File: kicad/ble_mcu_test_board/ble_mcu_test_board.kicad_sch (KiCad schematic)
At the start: 22 parts, among them J1 I2C, J2 SWD, U1 STM32WB10CCUx, U2 DLF162500LT-5028A1, Y1 32MHz

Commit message: prototype mobo progress
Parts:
- removed J1: I2C, symbol Connector:Conn_01x04_Pin
- removed J2: SWD, symbol Connector:Conn_01x04_Pin
- added AE1: Antenna, symbol Device:Antenna
- added C16: 0.3p, symbol Device:C
- added C17: 0.8p, symbol Device:C
- added C18, C19: 22u, symbol Device:C
- added J2: SWD, symbol Connector:Conn_01x04_Socket
- added J3: USB_C_Receptacle_PowerOnly_6P, symbol Connector:USB_C_Receptacle_PowerOnly_6P
- added J4: I2C_MUX_OUT, symbol Connector_Generic:Conn_02x16_Counter_Clockwise
- added L1: 2.7n, symbol Device:L
- added R3: 4k7, symbol Device:R
- added SW1: SW_SPDT, symbol Switch:SW_SPDT
- added U3: AMS1117-3.3, Package_TO_SOT_SMD:SOT-223-3_TabPin2, symbol Regulator_Linear:AMS1117-3.3
- added U4: TCA9548APWR, PW24_TEX, symbol 2024-09-17_00-23-00:TCA9548APWR
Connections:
- net +3.3V: now also C18.1, J4.12 (Pin_12), J4.16 (Pin_16), J4.17 (Pin_17), J4.21 (Pin_21), J4.25 (Pin_25), J4.29 (Pin_29), J4.4 (Pin_4), J4.8 (Pin_8), R3.1, U3.2 (VO), U4.24 (VCC)
- net GND: now also U2.2 (GND), U2.4 (GND), C16.2, C17.2, C18.2, C19.2, J2.4 (Pin_4), J3.A12 (GND), J3.B12 (GND), J4.1 (Pin_1), J4.13 (Pin_13), J4.20 (Pin_20), J4.24 (Pin_24), J4.28 (Pin_28), J4.32 (Pin_32), J4.5 (Pin_5), J4.9 (Pin_9), U3.1 (GND), U4.1 (A0), U4.12 (GND), U4.2 (A1), U4.21 (A2)
- net RF_OUT: now also C17.1, L1.1
- net at C10.1, C11.1, C4.1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: now also U1.1 (VBAT)
- net +3.3VA: now reaches C12.1, C13.1, U1.8 (VDDA)
- net at U2.1 (IN): now also C16.1, L1.2
- net at U2.3 (OUT): now also AE1.1 (A)
- net at R2.2, U1.6 (PB9): now also U4.23 (SDA)
- net at U1.39 (PA13): now also J2.2 (Pin_2)
- net BOOT0: now reaches U1.4 (PH3)
- net BOOT0: now also SW1.2 (B)
- net at U1.41 (PA14): now also J2.3 (Pin_3)
- net at R1.2, U1.5 (PB8): now also U4.22 (SCL)
- new net: R3.2, U4.3 (*RESET)
- new net: J4.10 (Pin_10), U4.16 (SC5)
- new net: J4.11 (Pin_11), U4.15 (SD5)
- new net: J4.14 (Pin_14), U4.14 (SC4)
- new net: J4.15 (Pin_15), U4.13 (SD4)
- new net: J4.18 (Pin_18), U4.11 (SC3)
- new net: J4.19 (Pin_19), U4.10 (SD3)
- new net: J4.2 (Pin_2), U4.20 (SC7)
- new net: J4.22 (Pin_22), U4.9 (SC2)
- new net: J4.23 (Pin_23), U4.8 (SD2)
- new net: J4.26 (Pin_26), U4.7 (SC1)
- new net: J4.27 (Pin_27), U4.6 (SD1)
- new net: J4.3 (Pin_3), U4.19 (SD7)
- new net: J4.30 (Pin_30), U4.5 (SC0)
- new net: J4.6 (Pin_6), U4.18 (SC6)
- new net: J4.7 (Pin_7), U4.17 (SD6)
- new net +3V3: J2.1 (Pin_1)
- new net VBUS: C19.1, J3.A9 (VBUS), J3.B9 (VBUS), U3.3 (VI)
- no-connect marks 0 -> 1
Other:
- note added: "2.4-2.5GHz LPF"
- note added: "Impedance matching network for QFN48 package STM32WB according to AN5165"
- note added: "POWER DECOUPLING"
- note added: "RF"
- note added: "nVDD x 100 nF + 1 x 4.7 μF"
- note removed: "Decoupling: nVDD x 100 nF + 1 x 4.7 μF"
- company: (none) -> FL24C6 / Posture Best
- title: (none) -> Bluetooth MCU Prototype
- moved on the sheet: C1, C10, C11, C12, C13, C14, C15, C2, C3, C4, C5, C6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

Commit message: finished schematic
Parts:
- added R4: 10k, symbol Device:R
- added SW2: SW_Push, symbol Switch:SW_Push
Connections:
- net +3V3 is gone; now on net +3.3V: J2.1 (Pin_1)
- net +3.3V: now also C10.1, C11.1, C14.1, C15.1, C4.1, C5.1, C6.1, C7.1, C8.1, C9.1, SW1.3 (C), U1.1 (VBAT), U1.20 (VDD), U1.23 (VDDRF), U1.31 (VDD), U1.33 (VDD), U1.34 (VDD), U1.35 (VDD), U1.40 (VDD), U1.48 (VDD)
- net BOOT0: now also R4.1; no longer SW1.2 (B)
- net GND: now also SW1.1 (A), SW2.2
- net at J4.31 (Pin_31): now also U4.4 (SD0)
- net at U1.15 (PA6): now also SW2.1
- new net: R4.2, SW1.2 (B)
- no-connect marks 1 -> 27
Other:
- note added: "BOOT MODE"
- note added: "Button for possible user control. Pulled up internally per STM32CubeIDE config."
- note added: "C1 and C2 must be connected to ground by separate vias."
- note added: "GND = Run code in flash 3.3V = Listen for peripherals"
- note added: "I2C"
- note added: "USB POWER"
- note removed: "C1 and C2 must be connected to ground by a separate via."
- moved on the sheet: C1, C10, C11, C12, C13, C14, C15, C2, C3, C4, C5, C6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

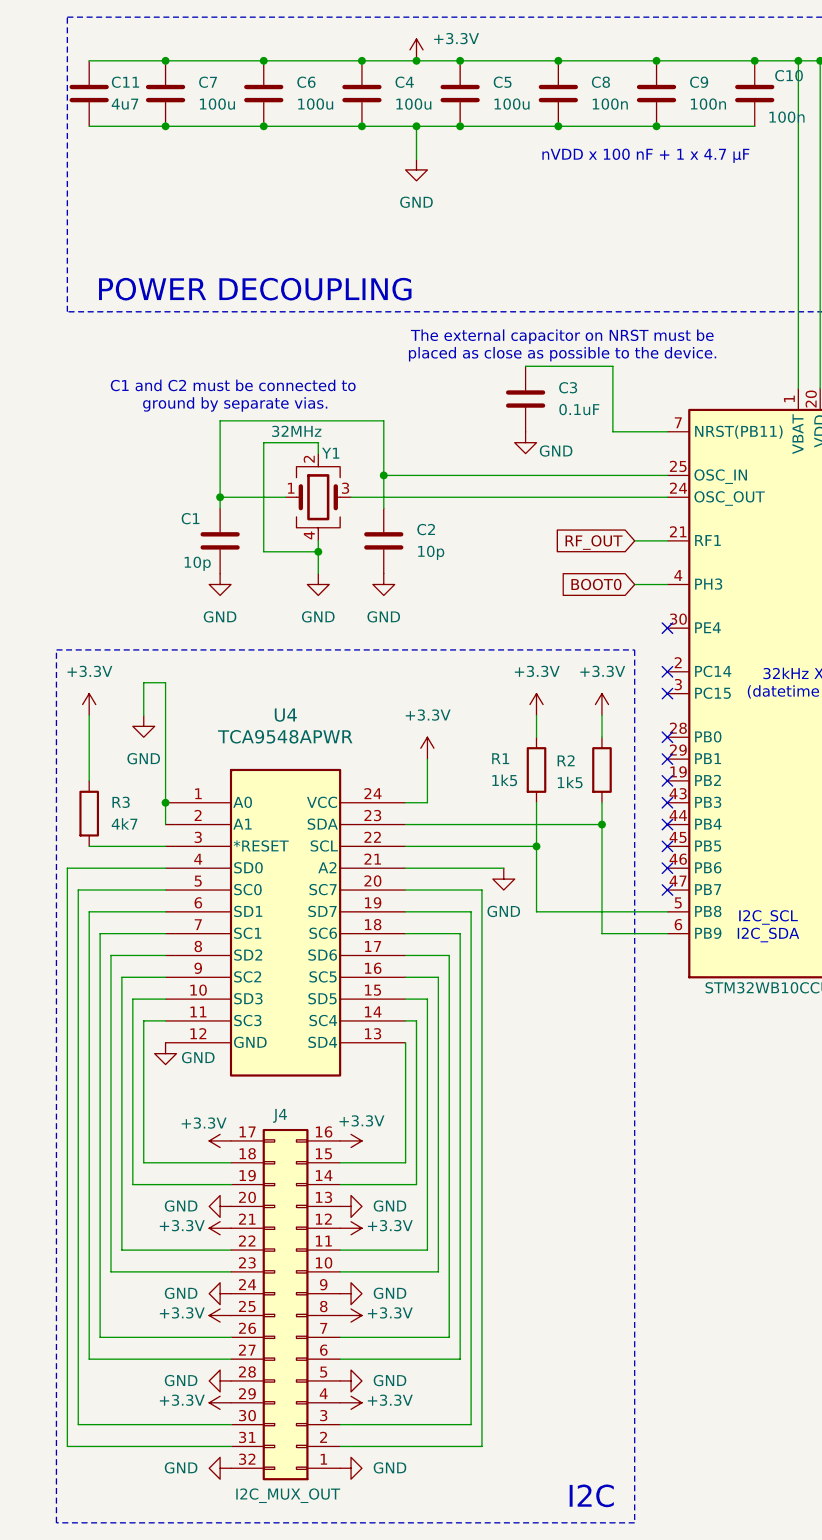
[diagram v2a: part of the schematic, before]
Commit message: reordered i2c multiplexer output, started pcb layout
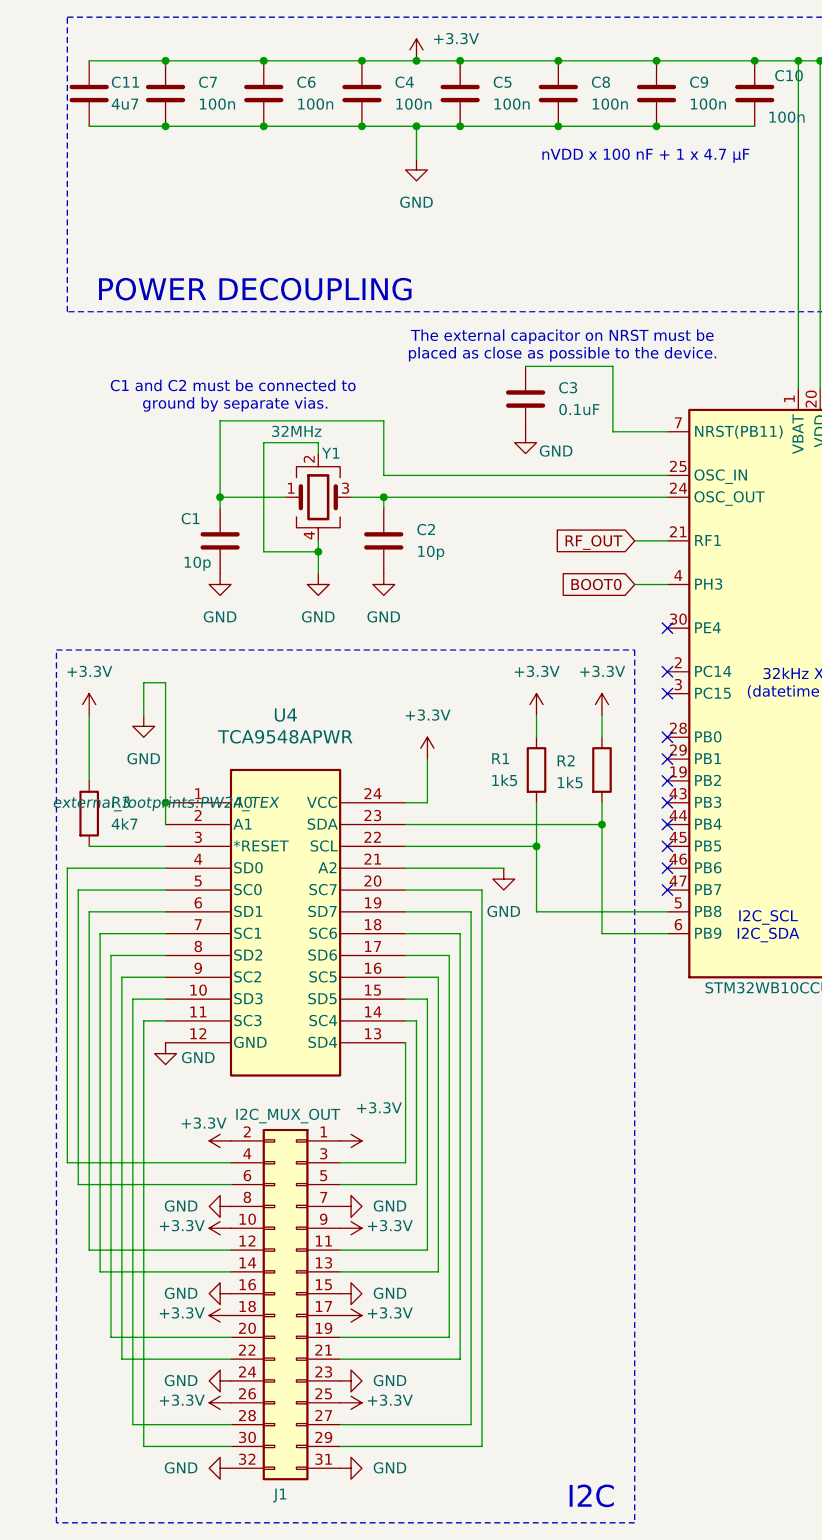
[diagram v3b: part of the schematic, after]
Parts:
- removed J4: I2C_MUX_OUT, symbol Connector_Generic:Conn_02x16_Counter_Clockwise
- added J1: I2C_MUX_OUT, Connector_PinSocket_2.54mm:PinSocket_2x16_P2.54mm_Horizontal, symbol Connector_Generic:Conn_02x16_Odd_Even
- C1, C10, C12, C13, C14, C15, C16, C17, C2, C3, C8, C9: footprint (none) -> Capacitor_SMD:C_0402_1005Metric
- C11: footprint (none) -> Capacitor_SMD:C_0603_1608Metric
- C18, C19: footprint (none) -> Capacitor_SMD:C_0805_2012Metric
- C4, C5, C6, C7: value 100u -> 100n; footprint (none) -> Capacitor_SMD:C_0402_1005Metric
- J2: footprint (none) -> Connector_PinSocket_2.54mm:PinSocket_1x04_P2.54mm_Horizontal
- R4: footprint (none) -> Resistor_SMD:R_0402_1005Metric_Pad0.72x0.64mm_HandSolder
- SW1: footprint (none) -> Button_Switch_SMD:SW_SPDT_PCM12
- SW2: footprint (none) -> Button_Switch_SMD:SW_Push_1P1T-SH_NO_CK_KMR2xxG
- U2: footprint DLF-4_1P6X0P8 -> external_footprints:DLF-4_1P6X0P8
- U4: footprint PW24_TEX -> external_footprints:PW24_TEX
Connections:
- net +3.3V: now also J1.1 (Pin_1), J1.10 (Pin_10), J1.17 (Pin_17), J1.18 (Pin_18), J1.2 (Pin_2), J1.25 (Pin_25), J1.26 (Pin_26), J1.9 (Pin_9)
- net GND: now also J1.15 (Pin_15), J1.16 (Pin_16), J1.23 (Pin_23), J1.24 (Pin_24), J1.31 (Pin_31), J1.32 (Pin_32), J1.7 (Pin_7), J1.8 (Pin_8)
- net at U4.16 (SC5): now also J1.13 (Pin_13)
- net at U4.15 (SD5): now also J1.11 (Pin_11)
- net at U4.14 (SC4): now also J1.5 (Pin_5)
- net at U4.13 (SD4): now also J1.3 (Pin_3)
- net at U4.11 (SC3): now also J1.30 (Pin_30)
- net at U4.10 (SD3): now also J1.28 (Pin_28)
- net at U4.20 (SC7): now also J1.29 (Pin_29)
- net at U4.9 (SC2): now also J1.22 (Pin_22)
- net at U4.8 (SD2): now also J1.20 (Pin_20)
- net at U4.7 (SC1): now also J1.14 (Pin_14)
- net at U4.6 (SD1): now also J1.12 (Pin_12)
- net at U4.19 (SD7): now also J1.27 (Pin_27)
- net at U4.5 (SC0): now also J1.6 (Pin_6)
- net at U4.4 (SD0): now also J1.4 (Pin_4)
- net at U4.18 (SC6): now also J1.21 (Pin_21)
- net at U4.17 (SD6): now also J1.19 (Pin_19)
- net at C1.1, U1.25 (OSC_IN), Y1.1: no longer C2.1
- net at U1.24 (OSC_OUT), Y1.3: now also C2.1

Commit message: prototype schematic + pcb finalized and ordered
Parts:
- added R5, R6: 5k1, Resistor_SMD:R_0603_1608Metric, symbol Device:R
- AE1: footprint (none) -> pcb_antenna:meander_antenna_stm32wb10cc
- J3: footprint (none) -> Connector_USB:USB_C_Receptacle_HRO_TYPE-C-31-M-17
- L1: footprint (none) -> Inductor_SMD:L_0402_1005Metric
- R1, R2: value 1k5 -> 4k7; footprint (none) -> Resistor_SMD:R_0603_1608Metric
- R3: footprint (none) -> Resistor_SMD:R_0402_1005Metric
- R4: footprint Resistor_SMD:R_0402_1005Metric_Pad0.72x0.64mm_HandSolder -> Resistor_SMD:R_0402_1005Metric
- SW1: footprint Button_Switch_SMD:SW_SPDT_PCM12 -> external_footprints:SW_SSSS811101
- Y1: footprint (none) -> Crystal:Crystal_SMD_2016-4Pin_2.0x1.6mm
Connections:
- net GND: now also R5.2, R6.1
- net at U1.39 (PA13): now also J2.3 (Pin_3); no longer J2.2 (Pin_2)
- net at U1.41 (PA14): now also J2.2 (Pin_2); no longer J2.3 (Pin_3)
- net at J3.A5 (CC1): now also R5.1
- net at J3.B5 (CC2): now also R6.2
- no-connect marks 27 -> 25
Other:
- note added: "Posture Best Prototype Mo-bo"
